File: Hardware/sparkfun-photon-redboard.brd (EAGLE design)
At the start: 68.6 x 53.3 mm, 54 parts, among them U1 WM-N-BM-14

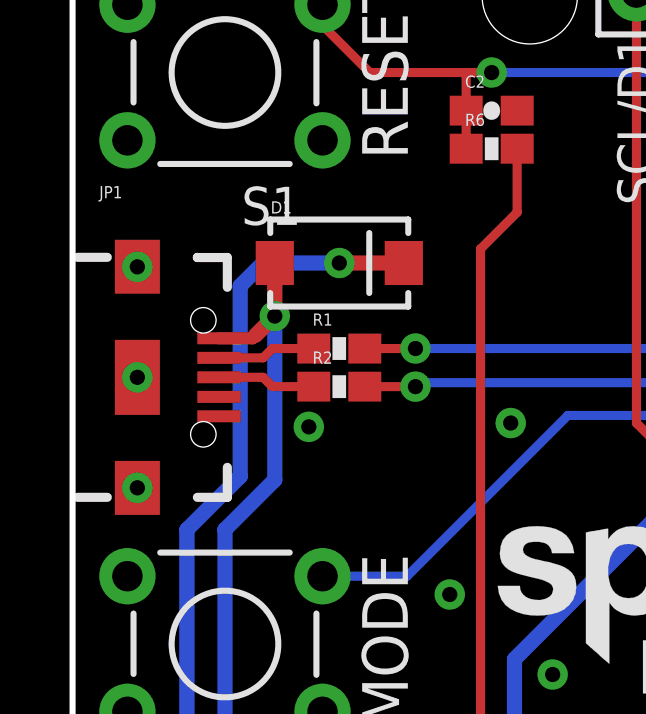
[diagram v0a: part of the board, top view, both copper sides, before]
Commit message: Photon Redboard with New USB Connector
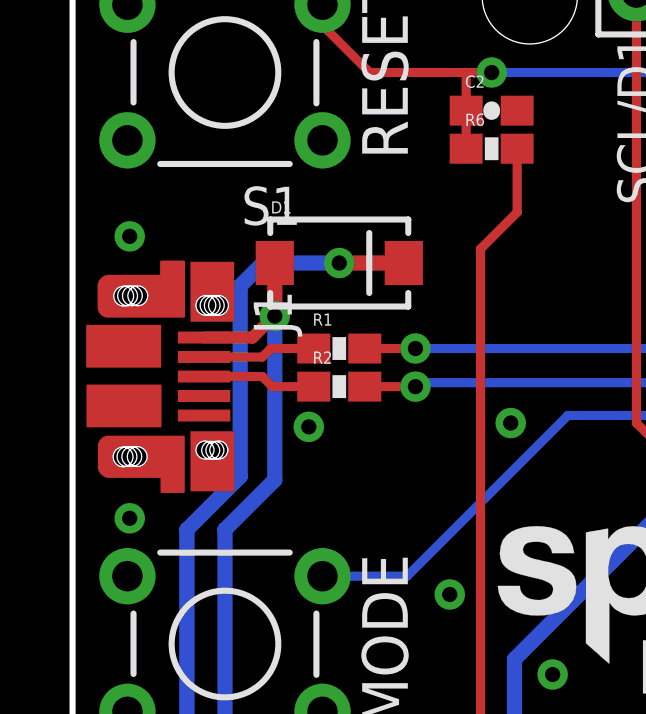
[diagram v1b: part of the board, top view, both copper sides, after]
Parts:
- removed JP1: USB, SparkFun-Connectors:USB-B-MICRO-SMD_V03
- added J1: USB-MICROB-PTH, SparkFun-Connectors:USB-MICROB-PTH
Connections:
- net D+: now also J1.D+; no longer JP1.D+1
- net D-: now also J1.D-; no longer JP1.D-1
- net GND: now also J1.GND, J1.SHIELD; no longer JP1.GND1, JP1.SHIELD1, JP1.SHIELD2, JP1.SHIELD3
- net VUSB: now also J1.VBUS; no longer JP1.VBUS1
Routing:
- net D+: track 3.28 -> 3.80 mm
- net GND: vias 29 -> 28
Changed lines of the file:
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@@
 <?xml version="1.0" encoding="utf-8"?>
 <!DOCTYPE eagle SYSTEM "eagle.dtd">
-<eagle version="7.1.0">
+<eagle version="7.7.0">
 <drawing>
 <settings>
@@
 <setting verticaltext="up"/>
 </settings>
-<grid distance="0.05" unitdist="inch" unit="inch" style="lines" multiple="1" display="yes" altdistance="0.005" altunitdist="inch" altunit="inch"/>
+<grid distance="0.01" unitdist="inch" unit="inch" style="lines" multiple="1" display="yes" altdistance="0.005" altunitdist="inch" altunit="inch"/>
 <layers>
 <layer number="1" name="Top" color="4" fill="1" visible="yes" active="yes"/>
@@
 <layer number="112" name="tSilk" color="7" fill="1" visible="no" active="yes"/>
 <layer number="113" name="IDFDebug" color="4" fill="1" visible="no" active="yes"/>
+<layer number="114" name="Badge_Outline" color="7" fill="1" visible="yes" active="yes"/>
+<layer number="115" name="ReferenceISLANDS" color="7" fill="1" visible="yes" active="yes"/>
 <layer number="116" name="Patch_BOT" color="9" fill="4" visible="no" active="yes"/>
+<layer number="118" name="Rect_Pads" color="7" fill="1" visible="yes" active="yes"/>
 <layer number="121" name="_tsilk" color="7" fill="1" visible="no" active="yes"/>
 <layer number="122" name="_bsilk" color="7" fill="1" visible="no" active="yes"/>
@@
 </autorouter>
 <elements>
-<element name="JP1" library="SparkFun-Connectors" package="USB-B-MICRO-SMD_V03" value="USB" x="2.159" y="38.1">
-<attribute name="PROD_ID" value="CONN-11752" x="2.159" y="38.1" size="1.778" layer="27" display="off"/>
-</element>
 <element name="R1" library="SparkFun-Resistors" package="0603-RES" value="22" x="8.89" y="39.06">
 <attribute name="PROD_ID" value="RES-08698" x="8.89" y="39.06" size="1.778" layer="27" font="vector" ratio="15" display="off"/>
@@
 <element name="SJ2" library="SparkFun-Passives" package="PAD-JUMPER-2-NC_BY_TRACE_YES_SILK" value="D7-LED" x="22.86" y="22.225" rot="MR0"/>
 <element name="LOGO3" library="SparkFun-Aesthetics" package="SFE_LOGO_NAME_FLAME_.4" value="SFE_LOGO_NAME_FLAME.4_INCH" x="40.64" y="6.35" rot="MR45"/>
+<element name="J1" library="SparkFun-Connectors" package="USB-MICROB-PTH" value="USB-MICROB-PTH" x="0.254" y="42.037" rot="R270">
+<attribute name="PROD_ID" value="CONN-XXXXXX" x="0.254" y="42.037" size="1.778" layer="27" rot="R270" display="off"/>
+</element>
 </elements>
 <signals>
 <signal name="GND">
-<contactref element="JP1" pad="SHIELD1"/>
-<contactref element="JP1" pad="SHIELD2"/>
-<contactref element="JP1" pad="SHIELD3"/>
-<contactref element="JP1" pad="GND1"/>
 <contactref element="C4" pad="2"/>
 <contactref element="C1" pad="C"/>
@@
 <contactref element="JP6" pad="14"/>
 <contactref element="JP6" pad="8"/>
-<via x="2.159" y="34.417" extent="1-16" drill="0.508"/>
-<via x="2.159" y="41.783" extent="1-16" drill="0.508"/>
-<via x="2.159" y="38.1" extent="1-16" drill="0.508"/>
+<via x="1.905" y="33.401" extent="1-16" drill="0.508"/>
+<via x="1.905" y="42.799" extent="1-16" drill="0.508"/>
 <wire x1="47.31" y1="12.09" x2="47.31" y2="11.237" width="0.508" layer="1"/>
 <via x="48.26" y="23.368" extent="1-16" drill="0.508"/>
@@
 <via x="16.002" y="28.194" extent="1-16" drill="0.508"/>
 <via x="26.67" y="33.274" extent="1-16" drill="0.508"/>
+<contactref element="J1" pad="GND"/>
+<contactref element="J1" pad="SHIELD"/>
 </signal>
 <signal name="3.3V">
@@
 </signal>
 <signal name="D-">
-<contactref element="JP1" pad="D-1"/>
 <contactref element="R1" pad="1"/>
-<wire x1="4.884" y1="38.75" x2="6.35" y2="38.75" width="0.3048" layer="1"/>
-<wire x1="6.35" y1="38.75" x2="6.66" y2="39.06" width="0.3048" layer="1"/>
-<wire x1="6.66" y1="39.06" x2="8.04" y2="39.06" width="0.3048" layer="1"/>
+<contactref element="J1" pad="D-"/>
+<wire x1="4.384" y1="38.777" x2="6.323" y2="38.777" width="0.3048" layer="1"/>
+<wire x1="8.04" y1="39.06" x2="6.606" y2="39.06" width="0.3048" layer="1"/>
+<wire x1="6.606" y1="39.06" x2="6.323" y2="38.777" width="0.3048" layer="1"/>
 </signal>
 <signal name="D+">
-<contactref element="JP1" pad="D+1"/>
 <contactref element="R2" pad="1"/>
-<wire x1="4.884" y1="38.1" x2="6.35" y2="38.1" width="0.3048" layer="1"/>
-<wire x1="6.35" y1="38.1" x2="6.66" y2="37.79" width="0.3048" layer="1"/>
-<wire x1="6.66" y1="37.79" x2="8.04" y2="37.79" width="0.3048" layer="1"/>
+<contactref element="J1" pad="D+"/>
+<wire x1="4.384" y1="38.127" x2="6.323" y2="38.127" width="0.3048" layer="1"/>
+<wire x1="6.323" y1="38.127" x2="6.66" y2="37.79" width="0.3048" layer="1"/>
+<wire x1="8.04" y1="37.79" x2="6.66" y2="37.79" width="0.3048" layer="1"/>
 </signal>
 <signal name="MCU_USB_D-">
@@
 </signal>
 <signal name="VUSB">
-<contactref element="JP1" pad="VBUS1"/>
 <contactref element="D1" pad="A"/>
 <contactref element="JP5" pad="5V"/>
-<wire x1="4.884" y1="39.4" x2="5.999" y2="39.4" width="0.4064" layer="1"/>
-<wire x1="5.999" y1="39.4" x2="6.096" y2="39.497" width="0.4064" layer="1"/>
-<wire x1="6.096" y1="39.497" x2="6.74" y2="40.141" width="0.508" layer="1"/>
 <via x="6.74" y="40.141" extent="1-16" drill="0.508"/>
 <wire x1="38.1" y1="2.667" x2="36.322" y2="0.889" width="0.508" layer="16"/>
@@
 <wire x1="11.43" y1="19.05" x2="11.43" y2="24.13" width="0.508" layer="16"/>
 <wire x1="11.43" y1="24.13" x2="10.668" y2="24.892" width="0.508" layer="16"/>
+<contactref element="J1" pad="VBUS"/>
+<wire x1="4.384" y1="39.427" x2="5.999" y2="39.427" width="0.4064" layer="1"/>
+<wire x1="6.74" y1="40.141" x2="6.713" y2="40.141" width="0.4064" layer="1"/>
+<wire x1="6.713" y1="40.141" x2="5.999" y2="39.427" width="0.4064" layer="1"/>
 </signal>
 <signal name="VIN">

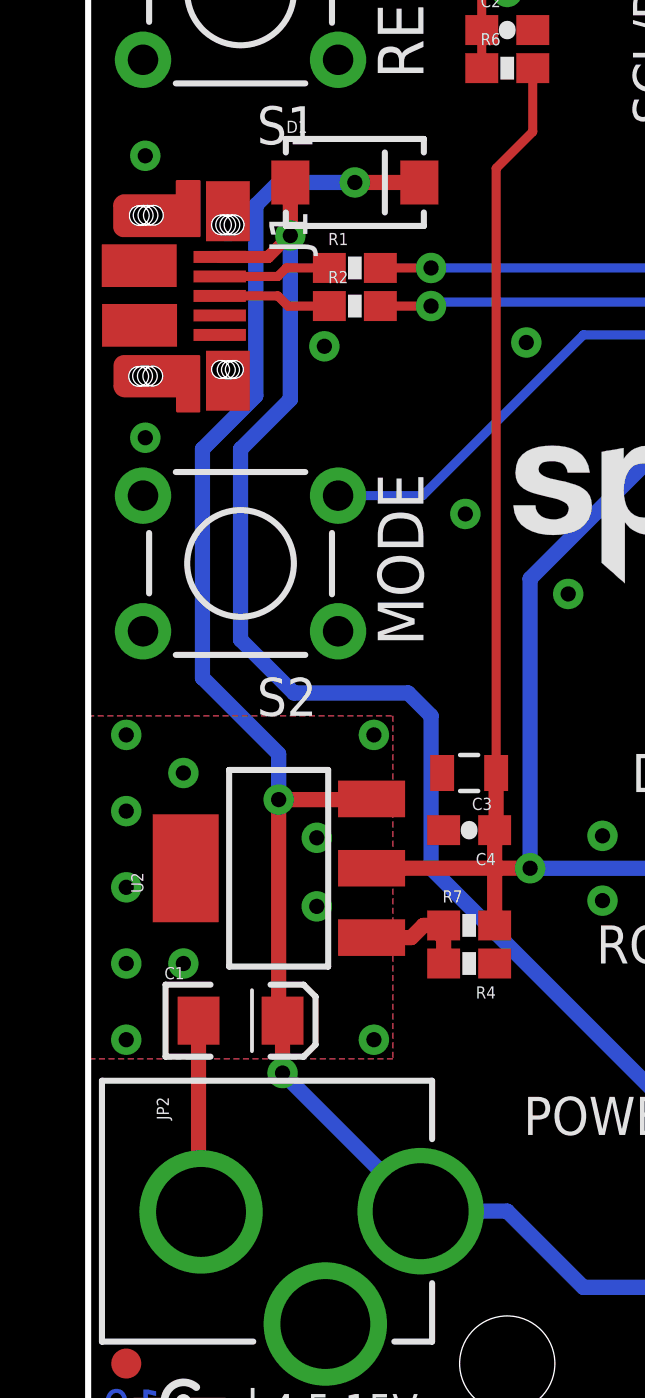
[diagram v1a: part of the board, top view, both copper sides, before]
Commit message: Updated USB package
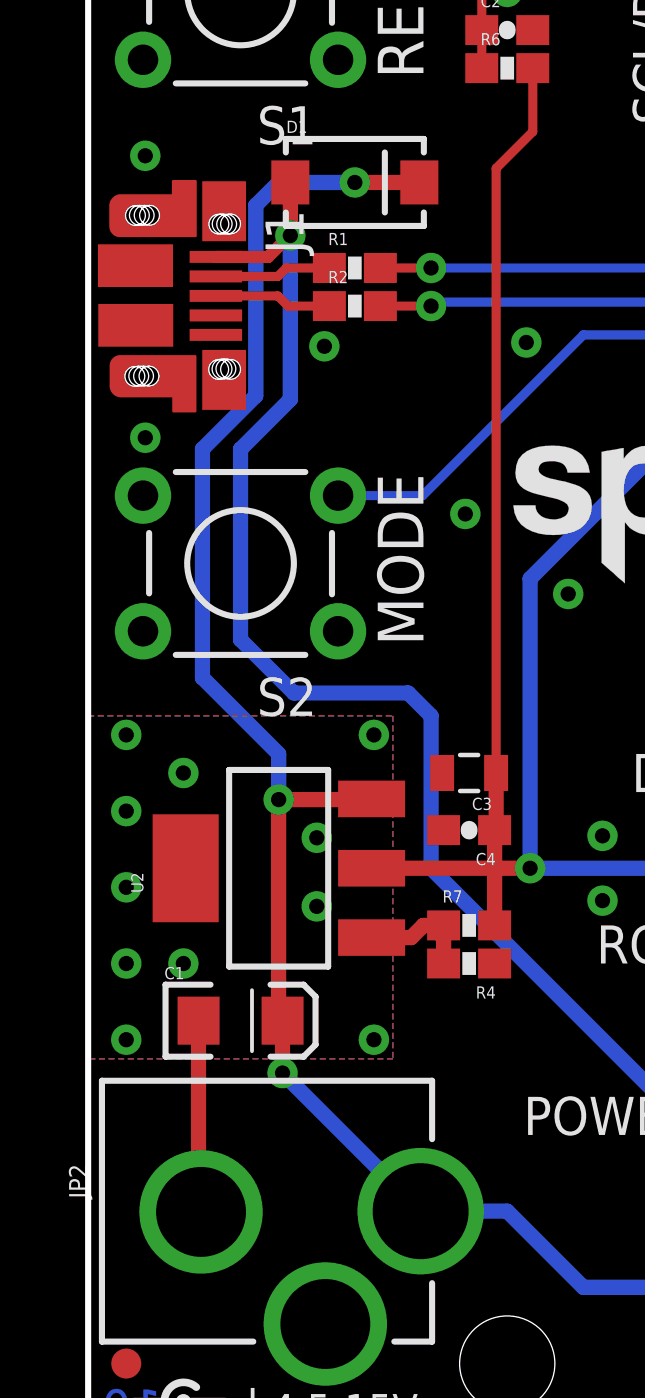
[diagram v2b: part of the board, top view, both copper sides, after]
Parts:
- moved J1 0.25 mm to (0.00, 42.0)
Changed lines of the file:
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@@
 <element name="SJ2" library="SparkFun-Passives" package="PAD-JUMPER-2-NC_BY_TRACE_YES_SILK" value="D7-LED" x="22.86" y="22.225" rot="MR0"/>
 <element name="LOGO3" library="SparkFun-Aesthetics" package="SFE_LOGO_NAME_FLAME_.4" value="SFE_LOGO_NAME_FLAME.4_INCH" x="40.64" y="6.35" rot="MR45"/>
-<element name="J1" library="SparkFun-Connectors" package="USB-MICROB-PTH" value="USB-MICROB-PTH" x="0.254" y="42.037" rot="R270">
-<attribute name="PROD_ID" value="CONN-XXXXXX" x="0.254" y="42.037" size="1.778" layer="27" rot="R270" display="off"/>
+<element name="J1" library="SparkFun-Connectors" package="USB-MICROB-PTH" value="USB-MICROB-PTH" x="0" y="42.037" rot="R270">
+<attribute name="PROD_ID" value="CONN-XXXXXX" x="0" y="42.037" size="1.778" layer="27" rot="R270" display="off"/>
 </element>
 </elements>
@@
 <contactref element="R1" pad="1"/>
 <contactref element="J1" pad="D-"/>
-<wire x1="4.384" y1="38.777" x2="6.323" y2="38.777" width="0.3048" layer="1"/>
+<wire x1="4.257" y1="38.777" x2="6.323" y2="38.777" width="0.3048" layer="1"/>
 <wire x1="8.04" y1="39.06" x2="6.606" y2="39.06" width="0.3048" layer="1"/>
 <wire x1="6.606" y1="39.06" x2="6.323" y2="38.777" width="0.3048" layer="1"/>
@@
 <contactref element="R2" pad="1"/>
 <contactref element="J1" pad="D+"/>
-<wire x1="4.384" y1="38.127" x2="6.323" y2="38.127" width="0.3048" layer="1"/>
+<wire x1="4.257" y1="38.127" x2="6.323" y2="38.127" width="0.3048" layer="1"/>
 <wire x1="6.323" y1="38.127" x2="6.66" y2="37.79" width="0.3048" layer="1"/>
 <wire x1="8.04" y1="37.79" x2="6.66" y2="37.79" width="0.3048" layer="1"/>
@@
 <wire x1="11.43" y1="24.13" x2="10.668" y2="24.892" width="0.508" layer="16"/>
 <contactref element="J1" pad="VBUS"/>
-<wire x1="4.384" y1="39.427" x2="5.999" y2="39.427" width="0.4064" layer="1"/>
+<wire x1="4.257" y1="39.427" x2="5.999" y2="39.427" width="0.4064" layer="1"/>
 <wire x1="6.74" y1="40.141" x2="6.713" y2="40.141" width="0.4064" layer="1"/>
 <wire x1="6.713" y1="40.141" x2="5.999" y2="39.427" width="0.4064" layer="1"/>
